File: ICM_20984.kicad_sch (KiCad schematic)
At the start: 8 parts, among them Q2 DMN65D8L, U10 ICM-20948, U9 AMS1117-1.8

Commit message: Nearly done schematics
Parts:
- removed Q2: DMN65D8L, Package_TO_SOT_SMD:SOT-23, symbol Transistor_FET:DMN67D7L
- added Q2, Q5: BSS138, Package_TO_SOT_SMD:SOT-23, symbol Transistor_FET:BSS138
- added R33, R34: 2.2k, Resistor_SMD:R_0402_1005Metric, symbol Device:R_Small_US
- renumbered C22 to C23, C23 to C24
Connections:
- net +1V8: now also Q2.1 (G), Q5.1 (G), R33.1
- net +3.3V: now also R34.1
- net Pico_SCL: now also Q5.2 (S), R33.2
- net Pico_SDA: now also Q2.2 (S)
- net SDA: now also Q2.3 (D)
- new net SCL: Q5.3 (D), R34.2

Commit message: Much much more progress
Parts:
- removed U9: AMS1117-1.8, Package_TO_SOT_SMD:SOT-223-3_TabPin2, symbol Regulator_Linear:AMS1117-1.8
- added C30, C31: 1uF, Capacitor_SMD:C_0201_0603Metric, symbol Device:C_Small
- added U13: MIC5365-3.3YC5, Package_TO_SOT_SMD:SOT-353_SC-70-5, symbol Regulator_Linear:MIC5365-3.3YC5
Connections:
- net +1V8: now also C31.1, U13.5 (VOUT)
- net +3.3V: now also C30.1, U13.1 (VIN), U13.3 (EN)
- net Earth: now also C30.2, C31.2, U13.2 (GND)
- net Pico_SCL: now also Q5.3 (D), R34.2; no longer Q5.2 (S), R33.2, U10.23 (SCL/SCLK)
- net Pico_SDA: now also Q2.3 (D), R23.2; no longer Q2.2 (S), R22.2, U10.24 (SDA/SDI)
- net SCL: now also Q5.2 (S), R33.2, U10.23 (SCL/SCLK); no longer Q5.3 (D), R34.2
- net SDA: now also Q2.2 (S), R22.2, U10.24 (SDA/SDI); no longer Q2.3 (D), R23.2

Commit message: clean up Rev
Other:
- moved on the sheet: C23, C24, C30, C31, Q2, Q5, R22, R23, R24, R33, R34, U10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

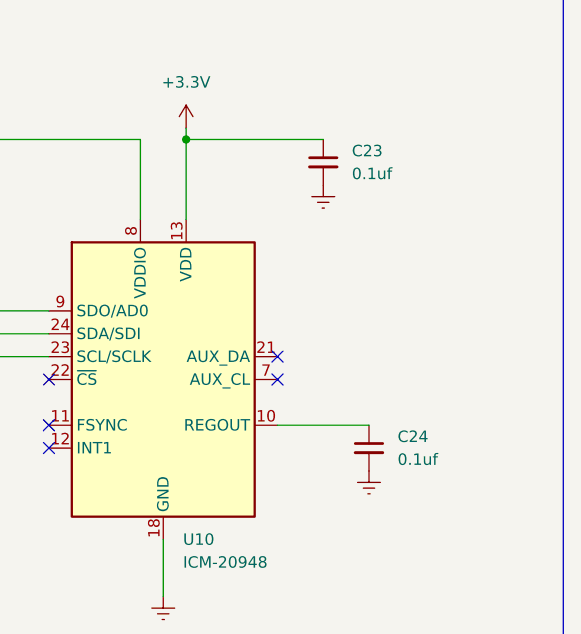
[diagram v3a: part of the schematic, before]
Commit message: Removed 201-sized parts
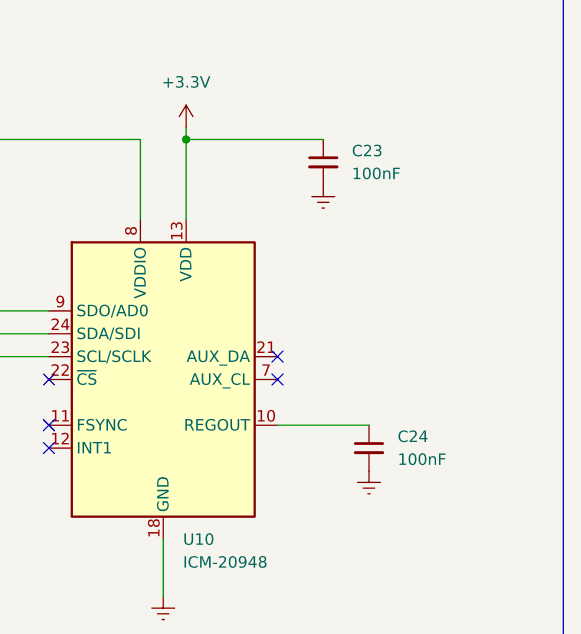
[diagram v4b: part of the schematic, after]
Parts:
- C23, C24: value 0.1uf -> 100nF
- C30, C31: footprint Capacitor_SMD:C_0201_0603Metric -> Capacitor_SMD:C_0402_1005Metric; LCSC Part # (none) -> C14445
- Q2, Q5: LCSC Part # (none) -> C52895
- R22, R23, R33, R34: LCSC Part # (none) -> C25933
- R24: LCSC Part # (none) -> C137973
- U10: LCSC Part # (none) -> C726001
- U13: LCSC Part # (none) -> C3021118
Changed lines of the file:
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@@
+      (effects (font (size 1.27 1.27)) hide)
+    )
+    (property "LCSC Part #" "C3021118" (at 157.861 87.122 0)
       (effects (font (size 1.27 1.27)) hide)
     )
@@
       (effects (font (size 1.27 1.27)) (justify left))
     )
-    (property "Footprint" "Capacitor_SMD:C_0201_0603Metric" (at 139.573 89.408 0)
+    (property "Footprint" "Capacitor_SMD:C_0402_1005Metric" (at 139.573 89.408 0)
       (effects (font (size 1.27 1.27)) hide)
     )
     (property "Datasheet" "~" (at 139.573 89.408 0)
+      (effects (font (size 1.27 1.27)) hide)
+    )
+    (property "LCSC Part #" "C14445" (at 139.573 89.408 0)
       (effects (font (size 1.27 1.27)) hide)
     )
@@
       (effects (font (size 1.27 1.27)) (justify left) hide)
     )
+    (property "LCSC Part #" "C52895" (at 78.613 91.821 0)
+      (effects (font (size 1.27 1.27)) hide)
+    )
     (pin "1")
     (pin "3")
@@
       (effects (font (size 1.27 1.27)) hide)
     )
+    (property "LCSC Part #" "C25933" (at 84.328 87.376 0)
+      (effects (font (size 1.27 1.27)) hide)
+    )
     (pin "1")
     (pin "2")
@@
       (effects (font (size 1.27 1.27)) hide)
     )
+    (property "LCSC Part #" "C25933" (at 69.088 86.741 0)
+      (effects (font (size 1.27 1.27)) hide)
+    )
     (pin "1")
     (pin "2")
@@
       (effects (font (size 1.27 1.27)) (justify left))
     )
-    (property "Value" "0.1uf" (at 222.123 120.1483 0)
+    (property "Value" "100nF" (at 222.123 120.1483 0)
       (effects (font (size 1.27 1.27)) (justify left))
     )
@@
       (effects (font (size 1.27 1.27)) hide)
     )
+    (property "LCSC Part #" "C137973" (at 169.418 103.632 0)
+      (effects (font (size 1.27 1.27)) hide)
+    )
     (pin "1")
     (pin "2")
@@
       (effects (font (size 1.27 1.27)) hide)
     )
+    (property "LCSC Part #" "C25933" (at 84.328 123.571 0)
+      (effects (font (size 1.27 1.27)) hide)
+    )
     (pin "1")
     (pin "2")
@@
     )
     (property "Datasheet" "http://www.invensense.com/wp-content/uploads/2016/06/DS-000189-ICM-20948-v1.3.pdf" (at 196.088 115.062 0)
+      (effects (font (size 1.27 1.27)) hide)
+    )
+    (property "LCSC Part #" "C726001" (at 196.088 111.252 0)
       (effects (font (size 1.27 1.27)) hide)
     )
@@
       (effects (font (size 1.27 1.27)) (justify left) hide)
     )
+    (property "LCSC Part #" "C52895" (at 78.613 128.016 0)
+      (effects (font (size 1.27 1.27)) hide)
+    )
     (pin "1")
     (pin "3")
@@
       (effects (font (size 1.27 1.27)) (justify left))
     )
-    (property "Value" "0.1uf" (at 217.043 88.3983 0)
+    (property "Value" "100nF" (at 217.043 88.3983 0)
       (effects (font (size 1.27 1.27)) (justify left))
     )
@@
     )
     (property "Datasheet" "~" (at 69.088 122.936 0)
+      (effects (font (size 1.27 1.27)) hide)
+    )
+    (property "LCSC Part #" "C25933" (at 69.088 122.936 0)
       (effects (font (size 1.27 1.27)) hide)
     )
@@
       (effects (font (size 1.27 1.27)) (justify left))
     )
-    (property "Footprint" "Capacitor_SMD:C_0201_0603Metric" (at 171.831 89.662 0)
+    (property "Footprint" "Capacitor_SMD:C_0402_1005Metric" (at 171.831 89.662 0)
       (effects (font (size 1.27 1.27)) hide)
     )
@@
       (effects (font (size 1.27 1.27)) hide)
     )
+    (property "LCSC Part #" "C14445" (at 171.831 89.662 0)
+      (effects (font (size 1.27 1.27)) hide)
+    )

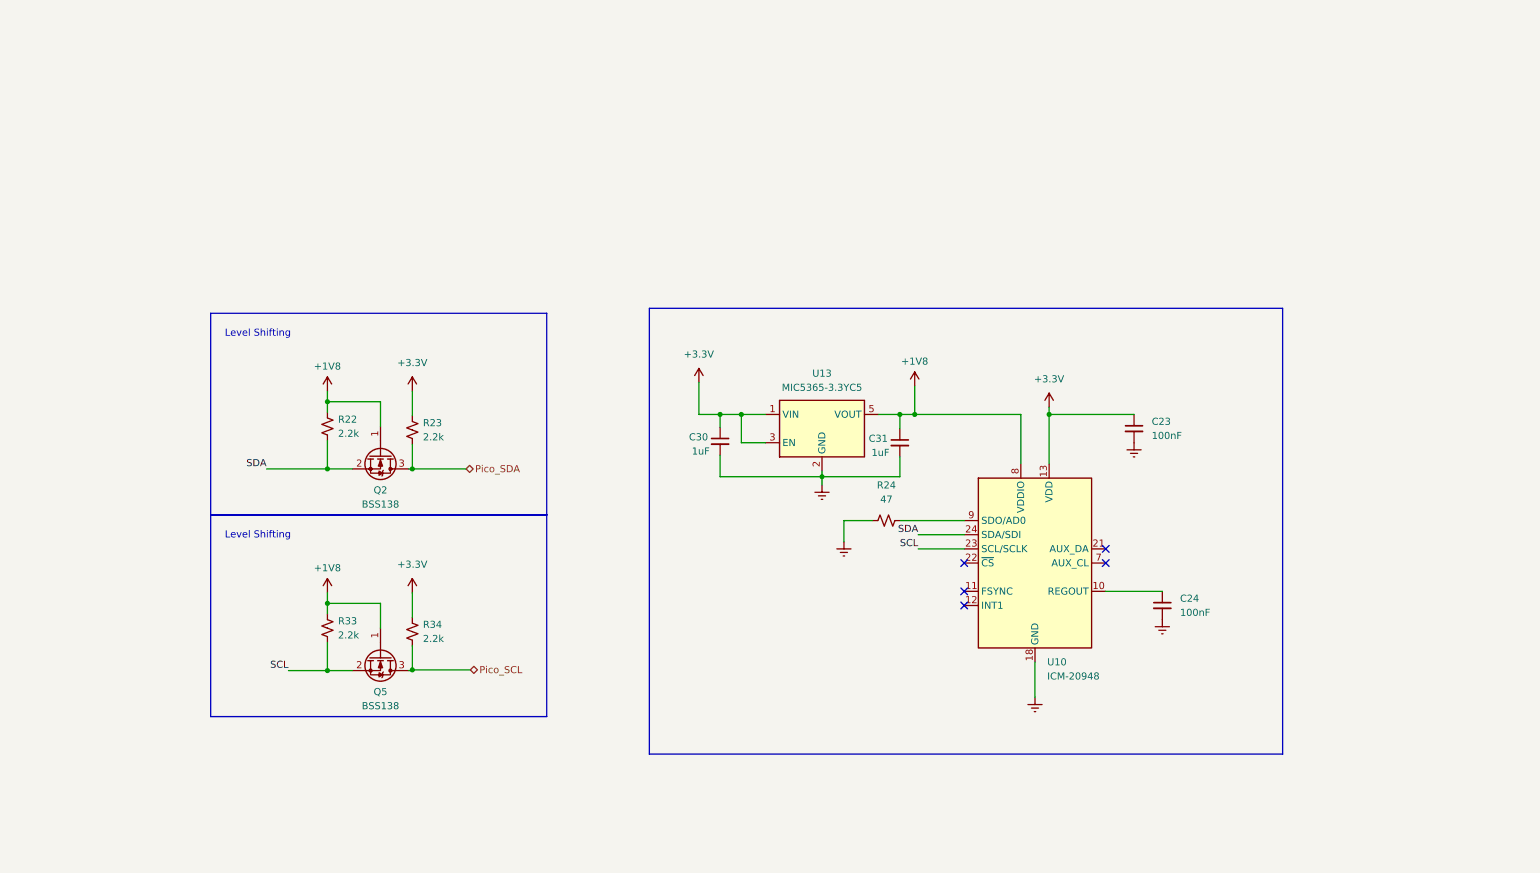
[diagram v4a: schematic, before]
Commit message: Replacing ICM-20948
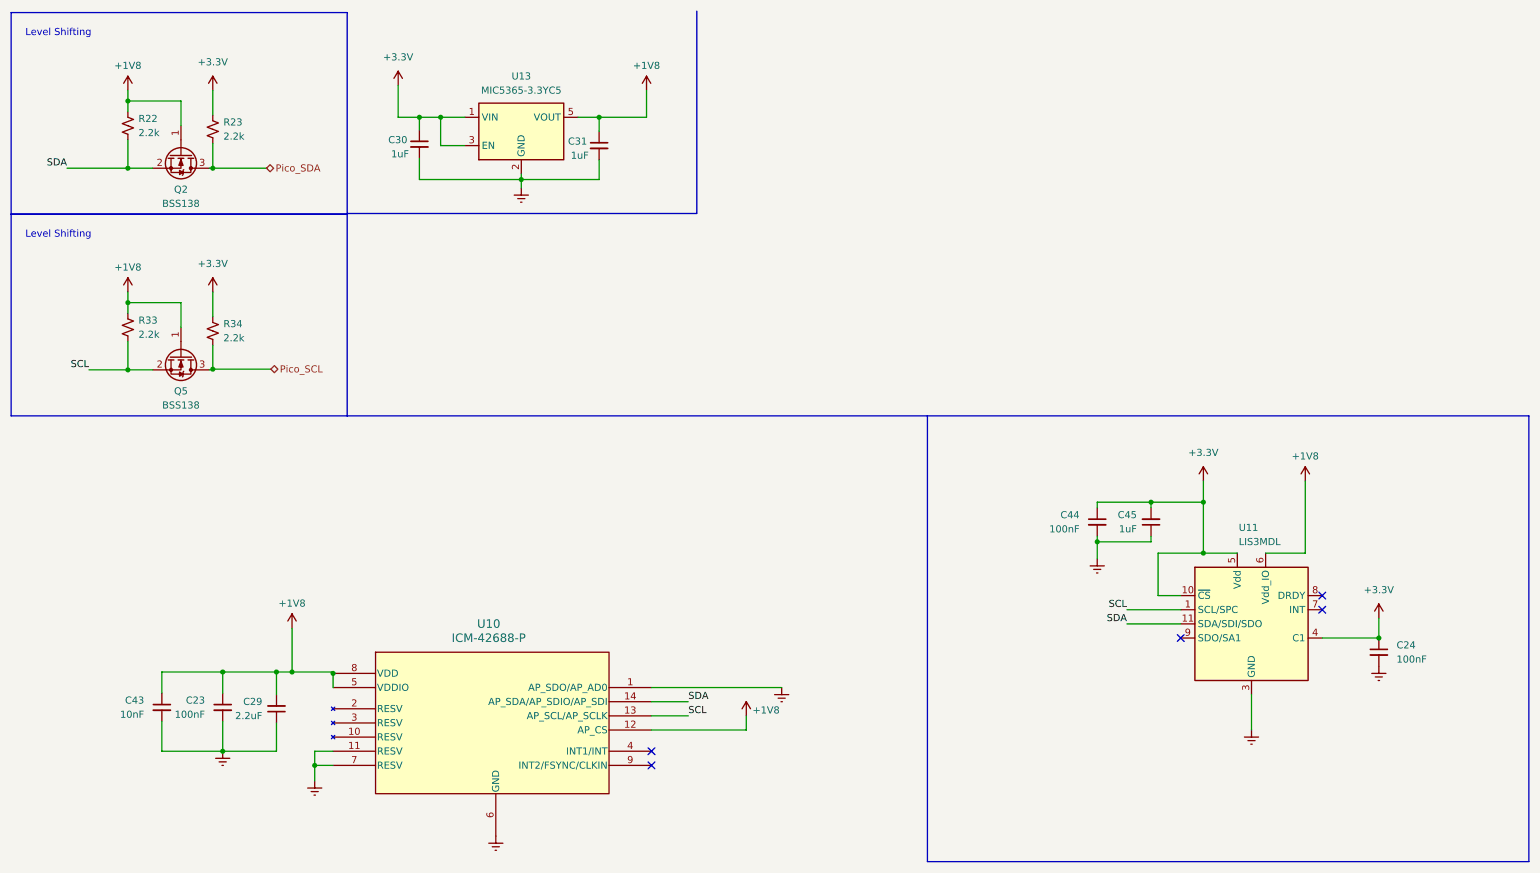
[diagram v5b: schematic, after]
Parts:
- removed R24: 47, Resistor_SMD:R_0402_1005Metric, symbol Device:R_Small_US
- removed U10: ICM-20948, Sensor_Motion:InvenSense_QFN-24_3x3mm_P0.4mm, symbol Sensor_Motion:ICM-20948
- added C29: 2.2uF, Capacitor_SMD:C_0402_1005Metric, symbol Device:C_Small
- added C43: 10nF, Capacitor_SMD:C_0402_1005Metric, symbol Device:C_Small
- added C44: 100nF, Capacitor_SMD:C_0402_1005Metric, symbol Device:C_Small
- added C45: 1uF, Capacitor_SMD:C_0402_1005Metric, symbol Device:C_Small
- added U10: ICM-42688-P, LGA14_2P5X3X0P91_TDK, symbol ICM-42688:ICM-42688-P
- added U11: LIS3MDL, Package_LGA:LGA-12_2x2mm_P0.5mm, symbol Sensor_Magnetic:LIS3MDL
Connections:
- net +1V8: now also C23.1, C29.2, C43.1, U10.12 (AP_CS), U10.5 (VDDIO), U10.8 (VDD), U11.6 (Vdd_IO)
- net +3.3V: now also C24.1, C44.1, C45.2, U11.10 (~{CS}), U11.4 (C1), U11.5 (Vdd); no longer C23.1
- net Earth: now also C29.1, C43.2, C44.2, C45.1, U10.1 (AP_SDO/AP_AD0), U10.11 (RESV), U10.6 (GND), U10.7 (RESV), U11.12 (GND), U11.2 (GND), U11.3 (GND)
- net SCL: now also U10.13 (AP_SCL/AP_SCLK), U11.1 (SCL/SPC)
- net SDA: now also U10.14 (AP_SDA/AP_SDIO/AP_SDI), U11.11 (SDA/SDI/SDO)
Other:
- moved on the sheet: C24, C30, C31, Q2, Q5, R22, R23, R33, R34, U13

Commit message: For production
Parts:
- C23, C24, C44: LCSC Part # (none) -> C1525
- C29: LCSC Part # (none) -> C12530
- C30, C31: LCSC Part # C14445 -> C52923
- C43: LCSC Part # (none) -> C15195
- C45: LCSC Part # (none) -> C52923
- R22, R23, R33, R34: LCSC Part # C25933 -> C25879
- U10: LCSC Part # (none) -> C1850418
- U11: LCSC Part # (none) -> C478483

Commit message: JLCniceness
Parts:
- U10: footprint LGA14_2P5X3X0P91_TDK -> ICM-42688:LGA14_2P5X3X0P91_TDK
- U11: JLCPCB Rotation Offset (none) -> 90
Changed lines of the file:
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@@
 			)
 		)
-		(property "JLCPCB Rotation Offset" ""
+		(property "JLCPCB Rotation Offset" "90"
 			(at 234.95 122.174 0)
 			(effects
@@
 			)
 		)
-		(property "Footprint" "LGA14_2P5X3X0P91_TDK"
+		(property "Footprint" "ICM-42688:LGA14_2P5X3X0P91_TDK"
 			(at 99.314 129.794 0)
 			(effects
